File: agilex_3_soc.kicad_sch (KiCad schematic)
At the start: 18 parts, among them J1 Conn_01x14, J2 Conn_02x03_Odd_Even, J3 Conn_02x19_Odd_Even, J4 Conn_01x03, J5 Conn_01x03, J6 Micro_SD_Card, J7 8P8C_LED_Shielded, U2 ADS7886xxDBV, U3 CD4051B, U5 IS43LQ32256A-062BLI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

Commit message: sketch io routing between connector and agilex
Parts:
- removed J6: Micro_SD_Card, Connector_Card:microSD_HC_Hirose_DM3AT-SF-PEJM5, symbol Connector:Micro_SD_Card
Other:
- moved on the sheet: U2, U3

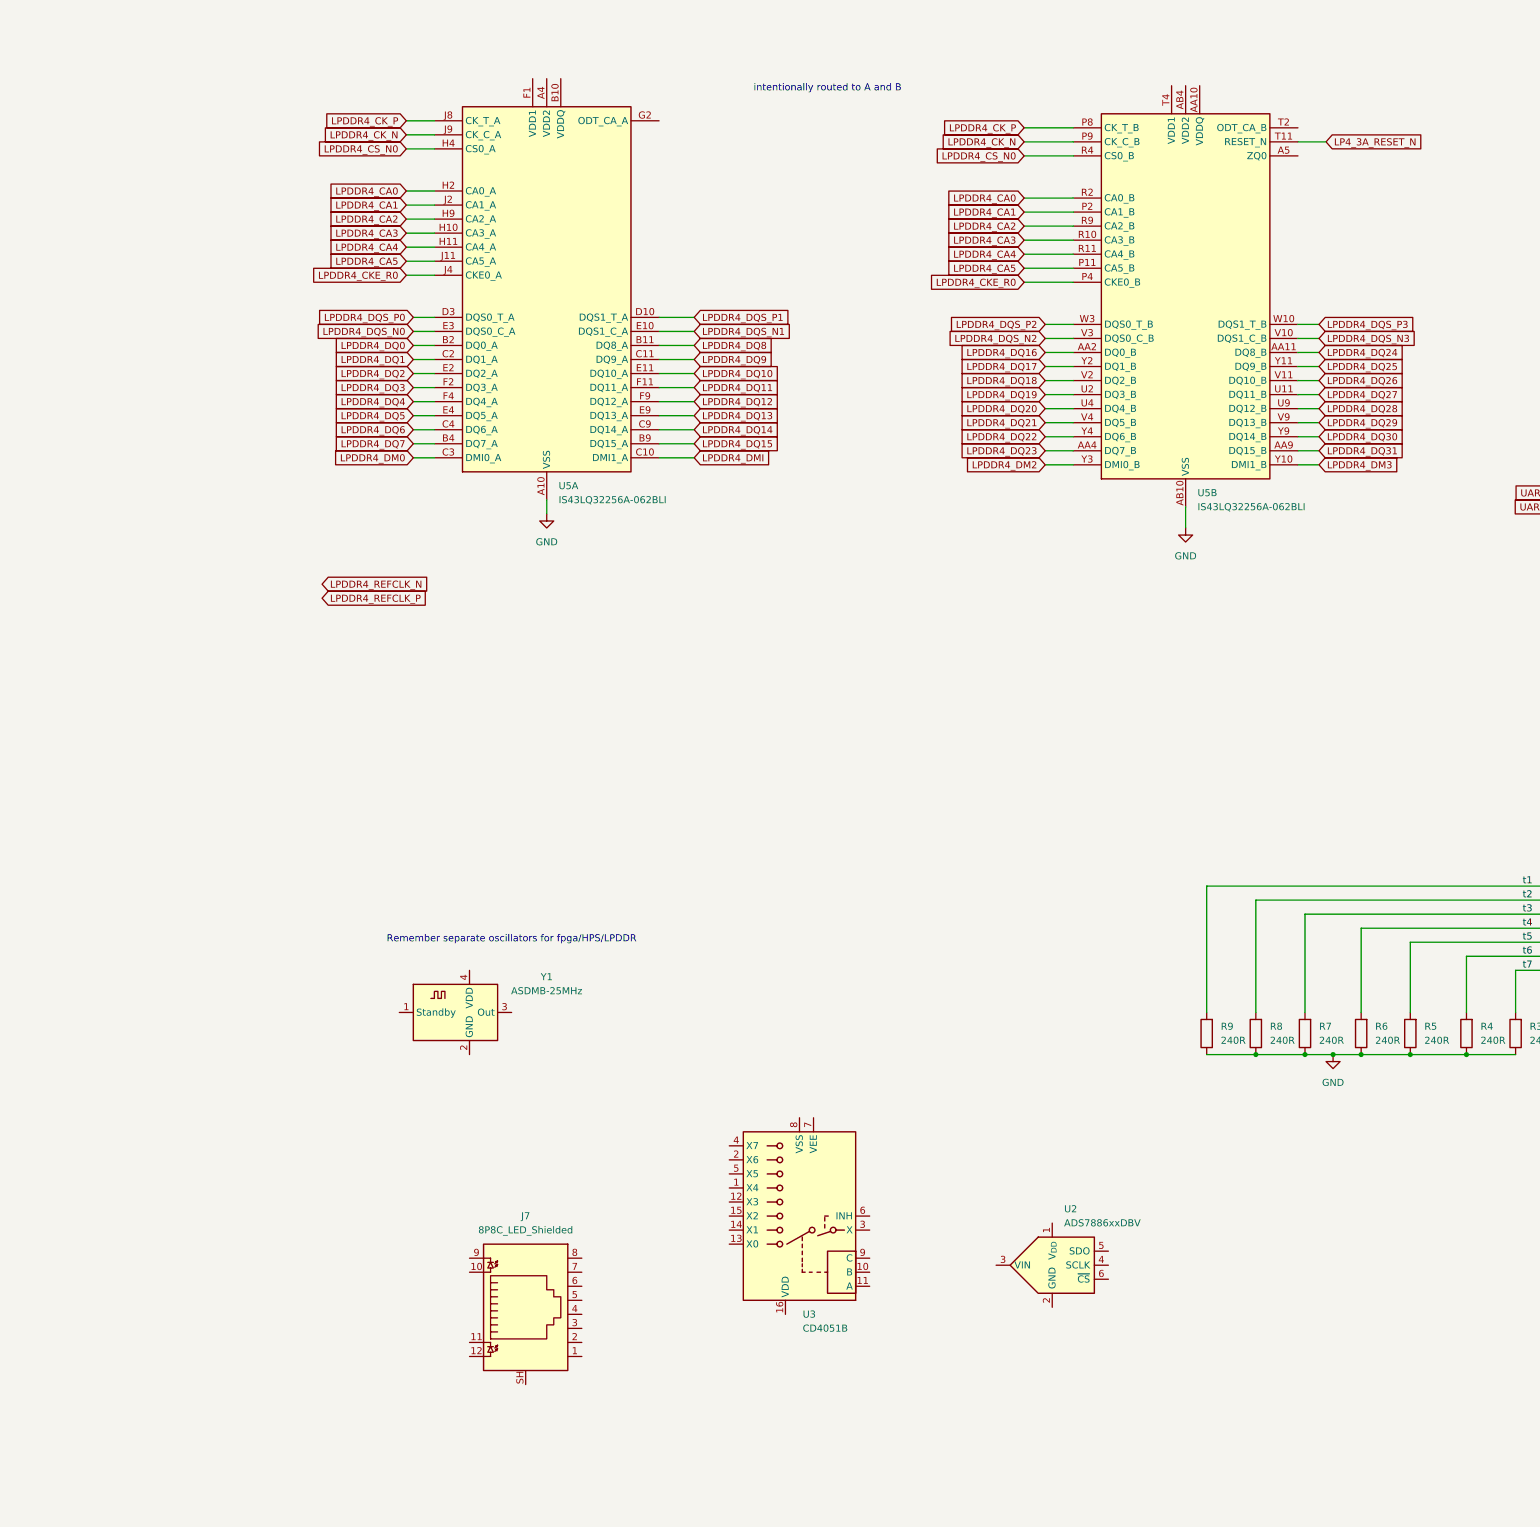
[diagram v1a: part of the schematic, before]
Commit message: move adc and admux to own schematic
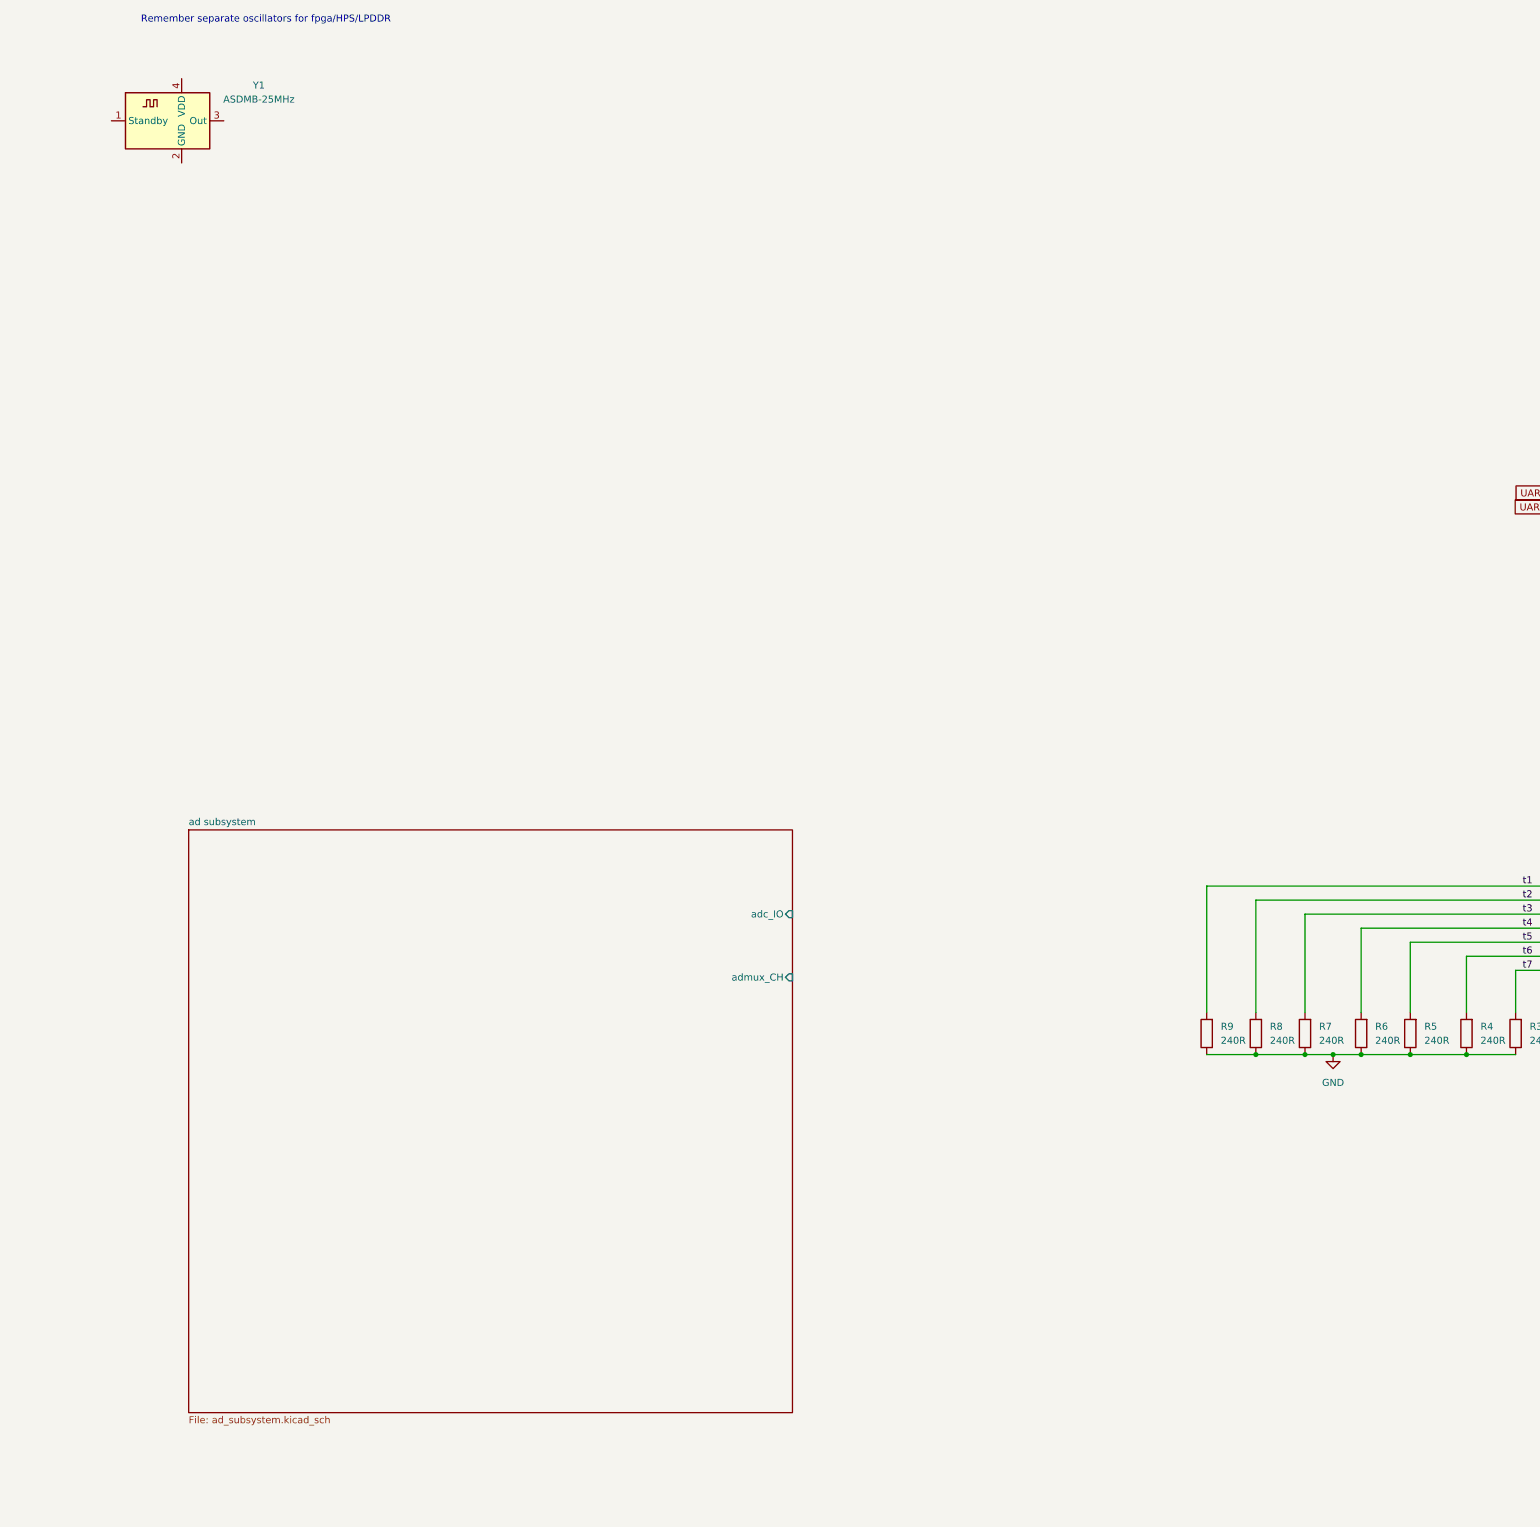
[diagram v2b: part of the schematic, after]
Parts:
- removed J7: 8P8C_LED_Shielded, Connector_RJ:RJ45_Bel_SI-60062-F, symbol Connector:8P8C_LED_Shielded
- removed U2: ADS7886xxDBV, Package_TO_SOT_SMD:SOT-23-6, symbol Analog_ADC:ADS7886xxDBV
- removed U3: CD4051B, Package_SO:TSSOP-16_4.4x5mm_P0.65mm, symbol Analog_Switch:CD4051B
- removed U5: IS43LQ32256A-062BLI, Package_BGA:BGA-200_10x14.5mm_Layout12x22_P0.8x0.65mm, symbol Memory_RAM:IS43LQ32256A-062BLI
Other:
- added sheet ad subsystem (ad_subsystem.kicad_sch)
- note removed: "intentionally routed to A and B"
- moved on the sheet: Y1

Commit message: try to figure out how to do buses
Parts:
- removed R3, R4, R5, R6, R7, R8, R9: 240R, Capacitor_SMD:C_0402_1005Metric, symbol Device:R
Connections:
- net GND: now also J3.34 (Pin_34), J3.37 (Pin_37)
- net ad_ch7: now reaches J3.35 (Pin_35)
- net ad_ch0: now reaches J3.36 (Pin_36)
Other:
- sheet ad subsystem ports: added {ad_ch}; removed admux_CH

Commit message: start adding power supplies
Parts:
- added J8: Conn_01x05, symbol Connector_Generic:Conn_01x05
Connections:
- net GND: now also J2.1 (Pin_1), J2.3 (Pin_3), J2.5 (Pin_5), J4.1 (Pin_1), J4.2 (Pin_2), J8.5 (Pin_5)

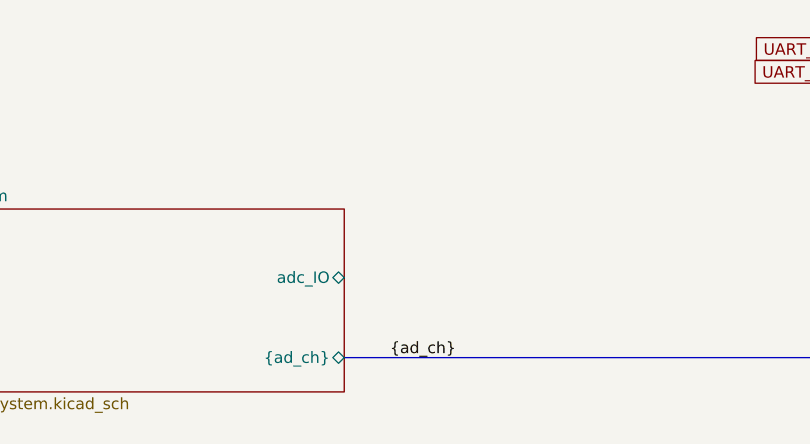
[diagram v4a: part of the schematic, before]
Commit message: add ads7056 footprint
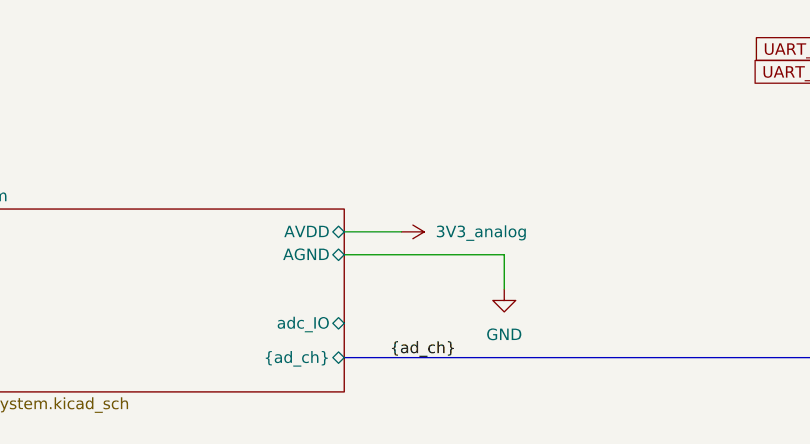
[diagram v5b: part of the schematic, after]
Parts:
- J8: footprint (none) -> Connector_PinHeader_2.54mm:PinHeader_1x05_P2.54mm_Vertical
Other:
- sheet ad subsystem ports: added AGND, AVDD; removed none
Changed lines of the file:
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@@
 	(wire
 		(pts
+			(xy 85.09 260.35) (xy 91.44 260.35)
+		)
+		(stroke
+			(width 0)
+			(type default)
+		)
+	)
+	(wire
+		(pts
 			(xy 256.54 231.14) (xy 256.54 233.68)
 		)
@@
 	(wire
 		(pts
+			(xy 102.87 266.7) (xy 102.87 262.89)
+		)
+		(stroke
+			(width 0)
+			(type default)
+		)
+	)
+	(wire
+		(pts
 			(xy 96.52 201.93) (xy 111.76 201.93)
 		)
@@
 		)
 	)
+	(wire
+		(pts
+			(xy 102.87 262.89) (xy 85.09 262.89)
+		)
+		(stroke
+			(width 0)
+			(type default)
+		)
+	)
 	(bus
 		(pts
@@
 	)
 	(symbol
+		(lib_id "power:GND")
+		(at 102.87 266.7 0)
+		(unit 1)
+		(body_style 1)
+		(exclude_from_sim no)
+		(in_bom yes)
+		(on_board yes)
+		(in_pos_files yes)
+		(dnp no)
+		(fields_autoplaced yes)
+		(property "Reference" "#PWR012"
+			(at 102.87 273.05 0)
+			(hide yes)
+			(show_name no)
+			(do_not_autoplace no)
+			(effects
+				(font
+					(size 1.27 1.27)
+				)
+			)
+		)
+		(property "Value" "GND"
+			(at 102.87 271.78 0)
+			(show_name no)
+			(do_not_autoplace no)
+			(effects
+				(font
+					(size 1.27 1.27)
+				)
+			)
+		)
+		(property "Footprint" ""
+			(at 102.87 266.7 0)
+			(hide yes)
+			(show_name no)
+			(do_not_autoplace no)
+			(effects
+				(font
+					(size 1.27 1.27)
+				)
+			)
+		)
+		(property "Datasheet" ""
+			(at 102.87 266.7 0)
+			(hide yes)
+			(show_name no)
+			(do_not_autoplace no)
+			(effects
+				(font
+					(size 1.27 1.27)
+				)
+			)
+		)
+		(property "Description" "Power symbol creates a global label with name \"GND\" , ground"
+			(at 102.87 266.7 0)
+			(hide yes)
+			(show_name no)
+			(do_not_autoplace no)
+			(effects
+				(font
+					(size 1.27 1.27)
+				)
+			)
+		)
+		(pin "1"
+		)
+		(instances
+			(project "agilex_3_soc"
+				(path "/a5b98d95-6877-4284-904f-d04e32723ae0"
+					(reference "#PWR012")
+					(unit 1)
+				)
+			)
+		)
+	)
+	(symbol
+		(lib_id "power:+1V1")
+		(at 91.44 260.35 270)
+		(unit 1)
+		(body_style 1)
+		(exclude_from_sim no)
+		(in_bom yes)
+		(on_board yes)
+		(in_pos_files yes)
+		(dnp no)
+		(property "Reference" "#PWR01214"
+			(at 87.63 260.35 0)
+			(hide yes)
+			(show_name no)
+			(do_not_autoplace no)
+			(effects
+				(font
+					(size 1.27 1.27)
+				)
+			)
+		)
+		(property "Value" "3V3_analog"
+			(at 95.25 260.3501 90)
+			(show_name no)
+			(do_not_autoplace no)
+			(effects
+				(font
+					(size 1.27 1.27)
+				)
+				(justify left)
+			)
+		)
+		(property "Footprint" ""
+			(at 91.44 260.35 0)
+			(hide yes)
+			(show_name no)
+			(do_not_autoplace no)
+			(effects
+				(font
+					(size 1.27 1.27)
+				)
+			)
+		)
+		(property "Datasheet" ""
+			(at 91.44 260.35 0)
+			(hide yes)
+			(show_name no)
+			(do_not_autoplace no)
+			(effects
+				(font
+					(size 1.27 1.27)
+				)
+			)
+		)
+		(property "Description" "Power symbol creates a global label with name \"+1V1\""
+			(at 91.44 260.35 0)
+			(hide yes)
+			(show_name no)
+			(do_not_autoplace no)
+			(effects
+				(font
+					(size 1.27 1.27)
+				)
+			)
+		)
+		(pin "1"
+		)
+		(instances
+			(project "agilex_3_soc"
+				(path "/a5b98d95-6877-4284-904f-d04e32723ae0"
+					(reference "#PWR01214")
+					(unit 1)
+				)
+			)
+		)
+	)
+	(symbol
 		(lib_id "Connector_Generic:Conn_02x03_Odd_Even")
 		(at 236.22 229.87 0)
@@
 			)
 		)
-		(property "Footprint" ""
+		(property "Footprint" "Connector_PinHeader_2.54mm:PinHeader_1x05_P2.54mm_Vertical"
 			(at 147.32 217.17 0)
 			(hide yes)
@@
 		)
 		(pin "adc_IO" bidirectional
-			(at 85.09 265.43 0)
+			(at 85.09 270.51 0)
 			(effects
 				(font
@@
 			(effects
 				(font
+					(size 1.27 1.27)
+				)
+				(justify right)
+			)
+		)
+		(pin "AGND" bidirectional
+			(at 85.09 262.89 0)
+			(effects
+				(font
+					(size 1.27 1.27)
+				)
+				(justify right)
+			)
+		)
+		(pin "AVDD" bidirectional
+			(at 85.09 260.35 0)
+			(effects
+				(font

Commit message: start routing sd card
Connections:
- net ad_ch1: now reaches J3.38 (Pin_38)
- net ad_ch7 renamed ad_ch2
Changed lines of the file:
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@@
-	)
-	(junction
-		(at 168.91 274.32)
-		(diameter 0)
-		(color 0 0 0 0)
 	)
 	(junction
@@
 		(color 0 0 0 0)
 	)
+	(junction
+		(at 163.83 274.32)
+		(diameter 0)
+		(color 0 0 0 0)
+	)
 	(bus_entry
-		(at 201.93 267.97)
-		(size 2.54 2.54)
-		(stroke
-			(width 0)
-			(type default)
-		)
-	)
-	(bus_entry
-		(at 171.45 265.43)
-		(size -2.54 2.54)
+		(at 204.47 270.51)
+		(size -2.54 -2.54)
 		(stroke
 			(width 0)
@@
 		)
 	)
+	(bus_entry
+		(at 163.83 267.97)
+		(size 2.54 -2.54)
+		(stroke
+			(width 0)
+			(type default)
+		)
+	)
 	(wire
 		(pts
@@
 	(wire
 		(pts
-			(xy 171.45 265.43) (xy 177.8 265.43)
-		)
-		(stroke
-			(width 0)
-			(type default)
-		)
-	)
-	(wire
-		(pts
 			(xy 63.5 125.73) (xy 78.74 125.73)
 		)
@@
 	(bus
 		(pts
-			(xy 168.91 274.32) (xy 204.47 274.32)
+			(xy 85.09 274.32) (xy 163.83 274.32)
 		)
 		(stroke
@@
 	(wire
 		(pts
+			(xy 190.5 267.97) (xy 201.93 267.97)
+		)
+		(stroke
+			(width 0)
+			(type default)
+		)
+	)
+	(wire
+		(pts
 			(xy 256.54 133.35) (xy 256.54 59.69)
 		)
@@
 		)
 	)
+	(bus
+		(pts
+			(xy 163.83 274.32) (xy 204.47 274.32)
+		)
+		(stroke
+			(width 0)
+			(type default)
+		)
+	)
 	(wire
 		(pts
@@
 	(wire
 		(pts
+			(xy 166.37 265.43) (xy 177.8 265.43)
+		)
+		(stroke
+			(width 0)
+			(type default)
+		)
+	)
+	(wire
+		(pts
 			(xy 96.52 199.39) (xy 111.76 199.39)
 		)
@@
 		)
 	)
-	(bus
-		(pts
-			(xy 204.47 270.51) (xy 204.47 274.32)
-		)
-		(stroke
-			(width 0)
-			(type default)
-		)
-	)
 	(wire
 		(pts
@@
 		)
 	)
+	(bus
+		(pts
+			(xy 163.83 264.16) (xy 163.83 274.32)
+		)
+		(stroke
+			(width 0)
+			(type default)
+		)
+	)
 	(wire
 		(pts
@@
 		)
 	)
-	(wire
-		(pts
-			(xy 190.5 267.97) (xy 201.93 267.97)
-		)
-		(stroke
-			(width 0)
-			(type default)
-		)
-	)
 	(bus
 		(pts
@@
 	(bus
 		(pts
-			(xy 204.47 267.97) (xy 204.47 270.51)
-		)
-		(stroke
-			(width 0)
-			(type default)
-		)
-	)
-	(bus
-		(pts
-			(xy 168.91 267.97) (xy 168.91 274.32)
+			(xy 204.47 267.97) (xy 204.47 274.32)
 		)
 		(stroke
@@
 		(pts
 			(xy 102.87 262.89) (xy 85.09 262.89)
-		)
-		(stroke
-			(width 0)
-			(type default)
-		)
-	)
-	(bus
-		(pts
-			(xy 85.09 274.32) (xy 168.91 274.32)
 		)
 		(stroke
@@
 		)
 	)
-	(label "ad_ch7"
-		(at 173.99 265.43 180)
-		(effects
-			(font
-				(size 1.27 1.27)
-			)
-			(justify right bottom)
-		)
-	)
 	(label "osc_clk_25"
 		(at 111.76 191.77 180)
@@
 		)
 	)
+	(label "ad_ch1"
+		(at 190.5 267.97 0)
+		(effects
+			(font
+				(size 1.27 1.27)
+			)
+			(justify left bottom)
+		)
+	)
 	(label "usb_clk24"
 		(at 111.76 214.63 180)
@@
 		)
 	)
+	(label "ad_ch2"
+		(at 170.18 265.43 0)
+		(effects
+			(font
+				(size 1.27 1.27)
+			)
+			(justify left bottom)
+		)
+	)

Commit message: more routes
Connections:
- net tms: now reaches J8.1 (Pin_1)
- net tdi: now reaches J8.2 (Pin_2)
- net tdo: now reaches J8.3 (Pin_3)
- net tck: now reaches J8.4 (Pin_4)
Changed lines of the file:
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@@
+	)
+	(bus_entry
+		(at 132.08 209.55)
+		(size 2.54 2.54)
+		(stroke
+			(width 0)
+			(type default)
+		)
 	)
 	(bus_entry
@@
 	)
 	(bus_entry
+		(at 132.08 212.09)
+		(size 2.54 2.54)
+		(stroke
+			(width 0)
+			(type default)
+		)
+	)
+	(bus_entry
+		(at 132.08 214.63)
+		(size 2.54 2.54)
+		(stroke
+			(width 0)
+			(type default)
+		)
+	)
+	(bus_entry
 		(at 163.83 267.97)
 		(size 2.54 -2.54)
@@
 		)
 	)
+	(bus_entry
+		(at 132.08 217.17)
+		(size 2.54 2.54)
+		(stroke
+			(width 0)
+			(type default)
+		)
+	)
 	(wire
 		(pts
@@
 		)
 	)
+	(wire
+		(pts
+			(xy 134.62 212.09) (xy 142.24 212.09)
+		)
+		(stroke
+			(width 0)
+			(type default)
+		)
+	)
 	(bus
 		(pts
@@
 	(wire
 		(pts
+			(xy 134.62 214.63) (xy 142.24 214.63)
+		)
+		(stroke
+			(width 0)
+			(type default)
+		)
+	)
+	(wire
+		(pts
 			(xy 140.97 240.03) (xy 143.51 240.03)
 		)
@@
 	(wire
 		(pts
+			(xy 134.62 217.17) (xy 142.24 217.17)
+		)
+		(stroke
+			(width 0)
+			(type default)
+		)
+	)
+	(wire
+		(pts
 			(xy 166.37 265.43) (xy 177.8 265.43)
 		)
@@
 	(wire
 		(pts
+			(xy 134.62 219.71) (xy 142.24 219.71)
+		)
+		(stroke
+			(width 0)
+			(type default)
+		)
+	)
+	(wire
+		(pts
 			(xy 259.08 90.17) (xy 259.08 135.89)
 		)
@@
 		(pts
 			(xy 204.47 267.97) (xy 204.47 274.32)
+		)
+		(stroke
+			(width 0)
+			(type default)
+		)
+	)
+	(bus
+		(pts
+			(xy 132.08 203.2) (xy 132.08 220.98)
 		)
 		(stroke
@@
 		)
 	)
+	(label "tms"
+		(at 137.16 212.09 0)
+		(effects
+			(font
+				(size 1.27 1.27)
+			)
+			(justify left bottom)
+		)
+	)
 	(label "{jtag}"
 		(at 68.58 49.53 0)
@@
 		)
 	)
+	(label "tdo"
+		(at 137.16 217.17 0)
+		(effects
+			(font
+				(size 1.27 1.27)
+			)
+			(justify left bottom)
+		)
+	)
+	(label "{jtag}"
+		(at 132.08 203.2 0)
+		(effects
+			(font
+				(size 1.27 1.27)
+			)
+			(justify left bottom)
+		)
+	)
 	(label "~{hpscold_rstn}"
 		(at 63.5 59.69 0)
@@
 		)
 	)
+	(label "tck"
+		(at 137.16 219.71 0)
+		(effects
+			(font
+				(size 1.27 1.27)
+			)
+			(justify left bottom)
+		)
+	)
 	(label "eth_clk25"
 		(at 114.3 57.15 0)
@@
 		(effects
 			(font
+				(size 1.27 1.27)
+			)
+			(justify left bottom)
+		)
+	)
+	(label "tdi"
+		(at 137.16 214.63 0)
+		(effects
+			(font
